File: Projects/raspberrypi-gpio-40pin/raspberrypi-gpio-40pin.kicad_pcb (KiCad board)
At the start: 2 copper layers, 65 x 56 mm, 5 parts, among them P1 Conn_02x20_Odd_Even

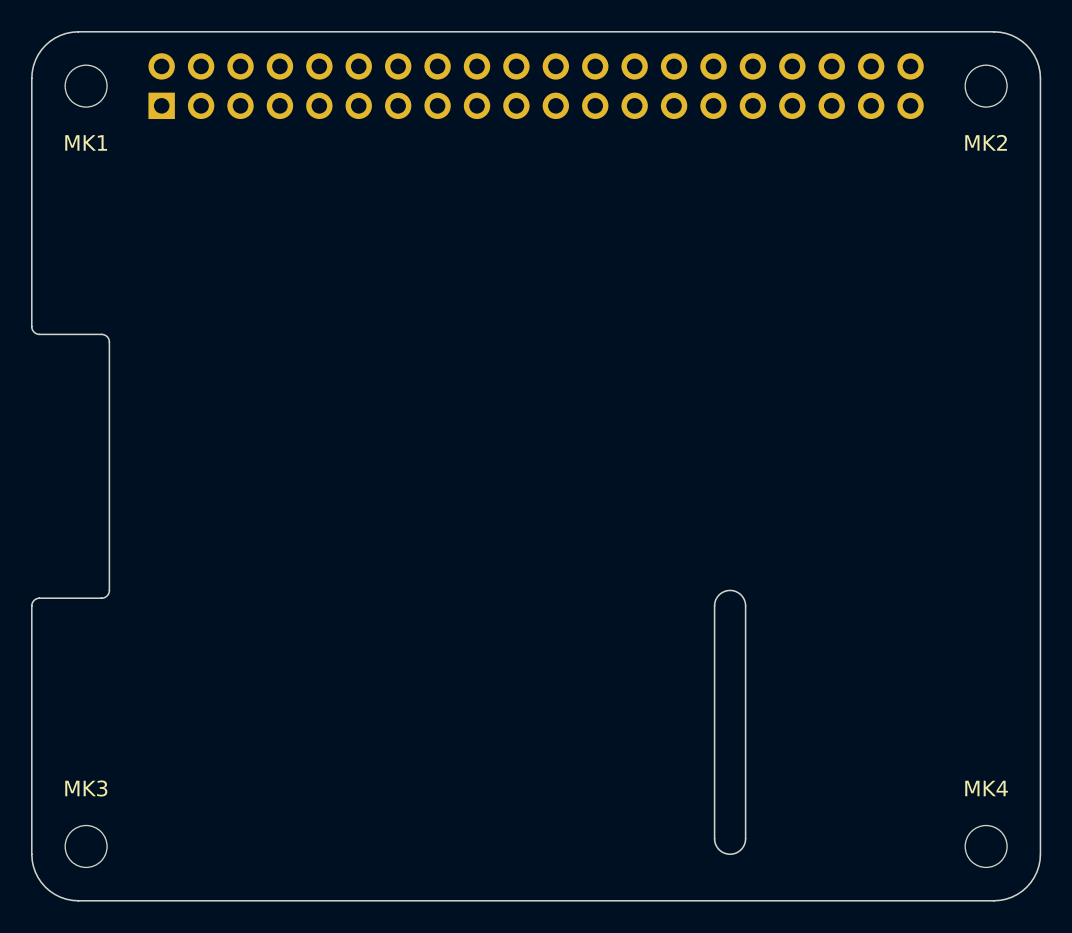
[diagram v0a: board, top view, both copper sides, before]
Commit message: Update raspberrypi-gpio-40pin using KiCad 5.1.6 * Revised .gitignore * Removed all *.net files * Repointed all symbols to current libraries * Updated documentation
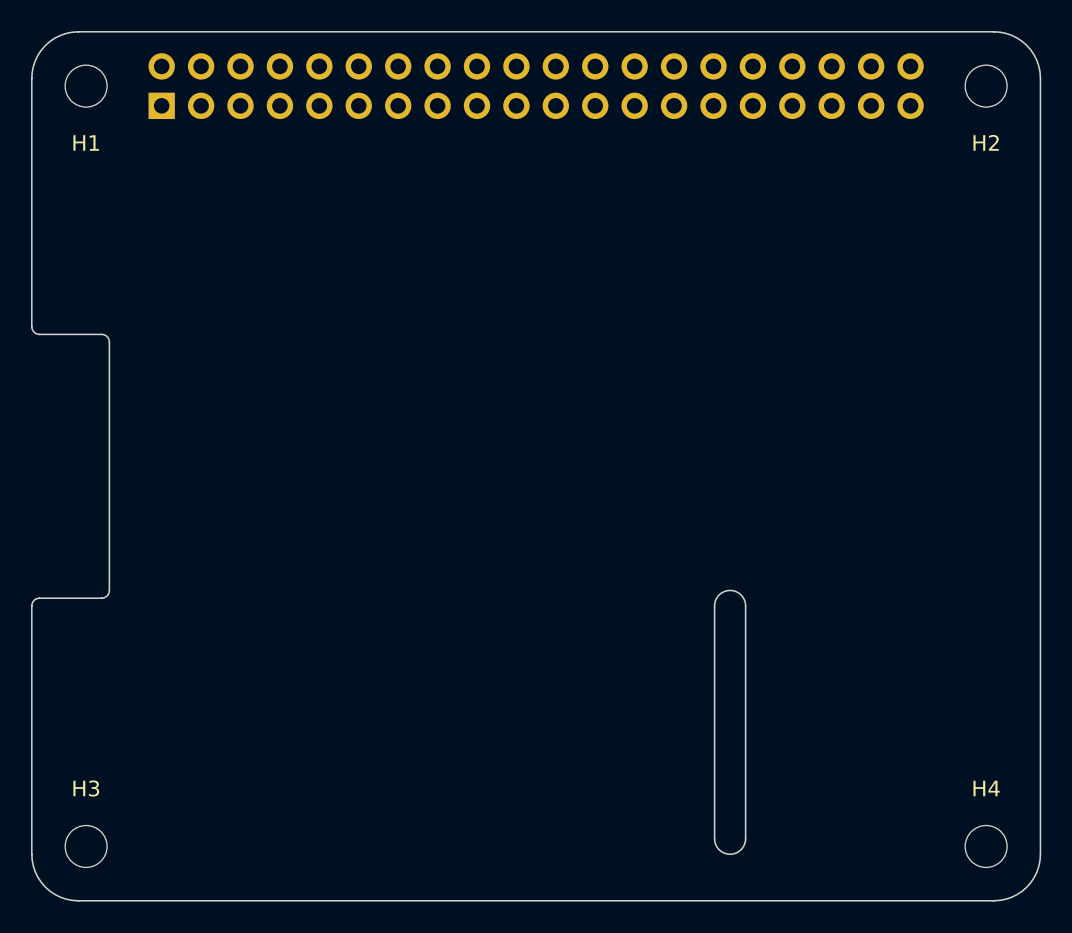
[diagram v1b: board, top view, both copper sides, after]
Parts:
- renumbered MK1 to H1, MK2 to H2, MK3 to H3, MK4 to H4, P1 to J1
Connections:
- J1 pad 10: /GPIO15(RXD0) -> (no net)
- J1 pad 11: /GPIO17(GEN0) -> (no net)
- J1 pad 12: /GPIO18(GEN1)(PWM0) -> (no net)
- J1 pad 13: /GPIO27(GEN2) -> (no net)
- J1 pad 15: /GPIO22(GEN3) -> (no net)
- J1 pad 16: /GPIO23(GEN4) -> (no net)
- J1 pad 18: /GPIO24(GEN5) -> (no net)
- J1 pad 19: /GPIO10(SPI0_MOSI) -> (no net)
- J1 pad 21: /GPIO9(SPI0_MISO) -> (no net)
- J1 pad 22: /GPIO25(GEN6) -> (no net)
- J1 pad 23: /GPIO11(SPI0_SCK) -> (no net)
- J1 pad 24: /GPIO8(SPI0_CE_N) -> (no net)
- J1 pad 26: /GPIO7(SPI1_CE_N) -> (no net)
- J1 pad 27: /ID_SD -> (no net)
- J1 pad 28: /ID_SC -> (no net)
- J1 pad 29: /GPIO5 -> (no net)
- J1 pad 3: /GPIO2(SDA1) -> (no net)
- J1 pad 31: /GPIO6 -> (no net)
- J1 pad 32: /GPIO12(PWM0) -> (no net)
- J1 pad 33: /GPIO13(PWM1) -> (no net)
- J1 pad 35: /GPIO19(SPI1_MISO) -> (no net)
- J1 pad 36: /GPIO16 -> (no net)
- J1 pad 37: /GPIO26 -> (no net)
- J1 pad 38: /GPIO20(SPI1_MOSI) -> (no net)
- J1 pad 40: /GPIO21(SPI1_SCK) -> (no net)
- J1 pad 5: /GPIO3(SCL1) -> (no net)
- J1 pad 7: /GPIO4(GCLK) -> (no net)
- J1 pad 8: /GPIO14(TXD0) -> (no net)
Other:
- board text added: "RASPBERRY PI 40-PIN ADDON BOARD VIEW FROM TOP NOTE: J1 SHOULD BE FITTED ON THE REVERSE OF THE BOARD ADD EDGE CUTS FROM CAMERA AND DISPLAY PORTS AS REQUIRED"
- board text removed: "RASPBERRY-PI 40-PIN ADDON BOARD VIEW FROM TOP NOTE: P1 SHOULD BE FITTED ON THE REVERSE OF THE BOARD ADD EDGE CUTS FROM CAMERA AND DISPLAY PORTS AS REQUIRED"
